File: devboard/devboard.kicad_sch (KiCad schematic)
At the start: 22 parts, among them J1 USB_C_Receptacle_USB2.0_14P, U1 RP2040, U2 NCP1117-3.3_SOT223, Y1 Crystal_GND24

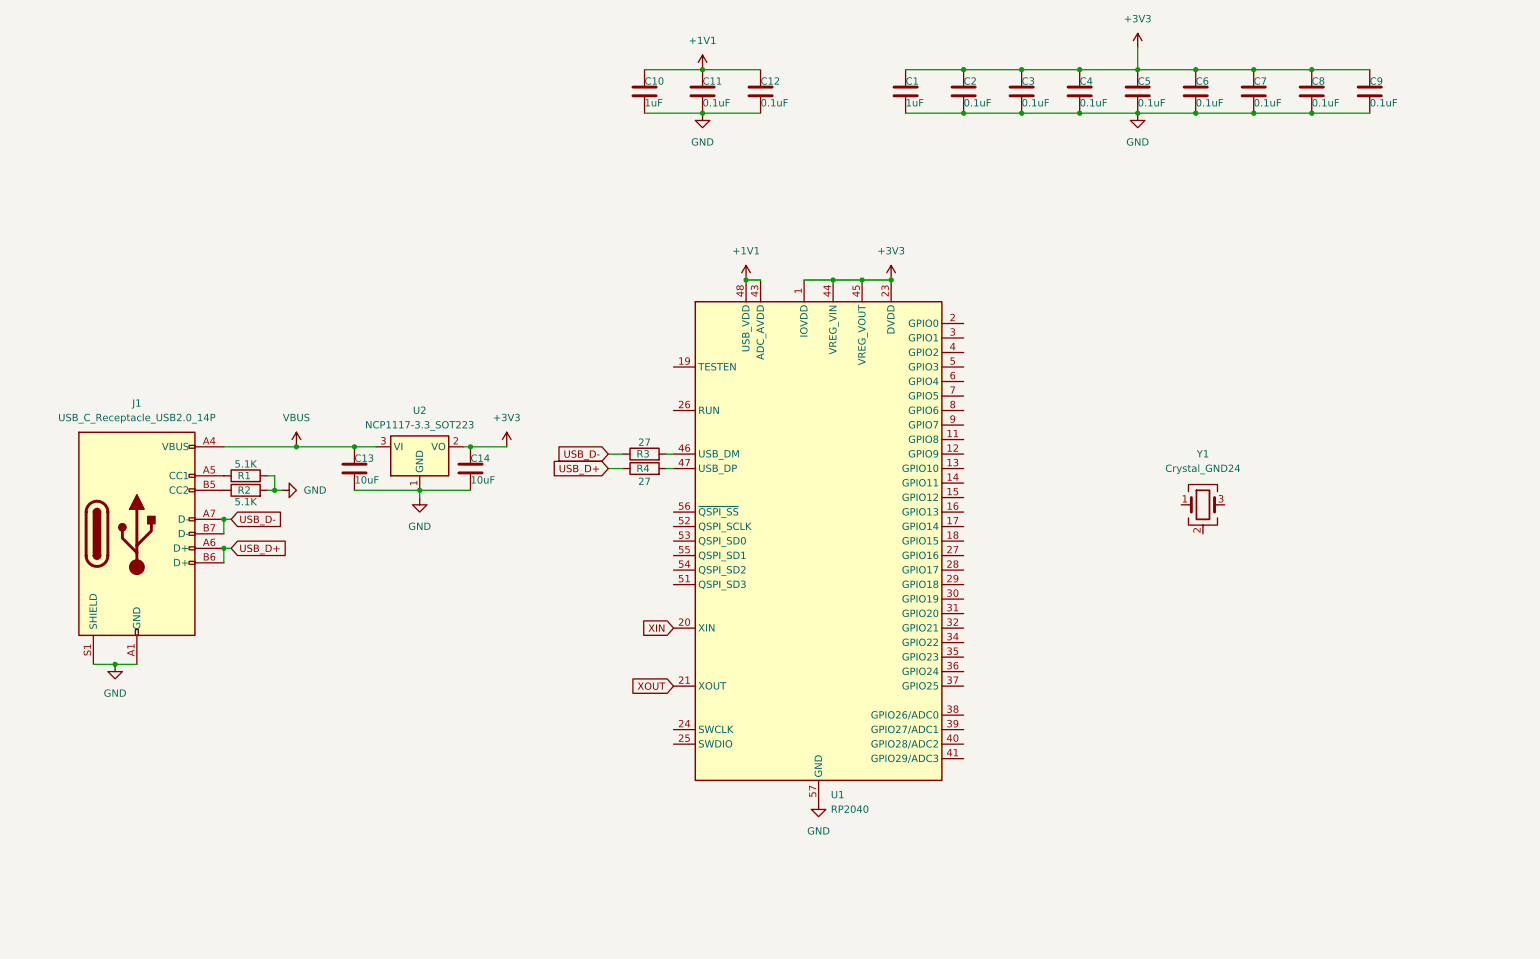
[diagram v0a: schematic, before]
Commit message: Finished basic schematic of Devboard 1.0
The schematics of the devboard with basic functionalities was finished.
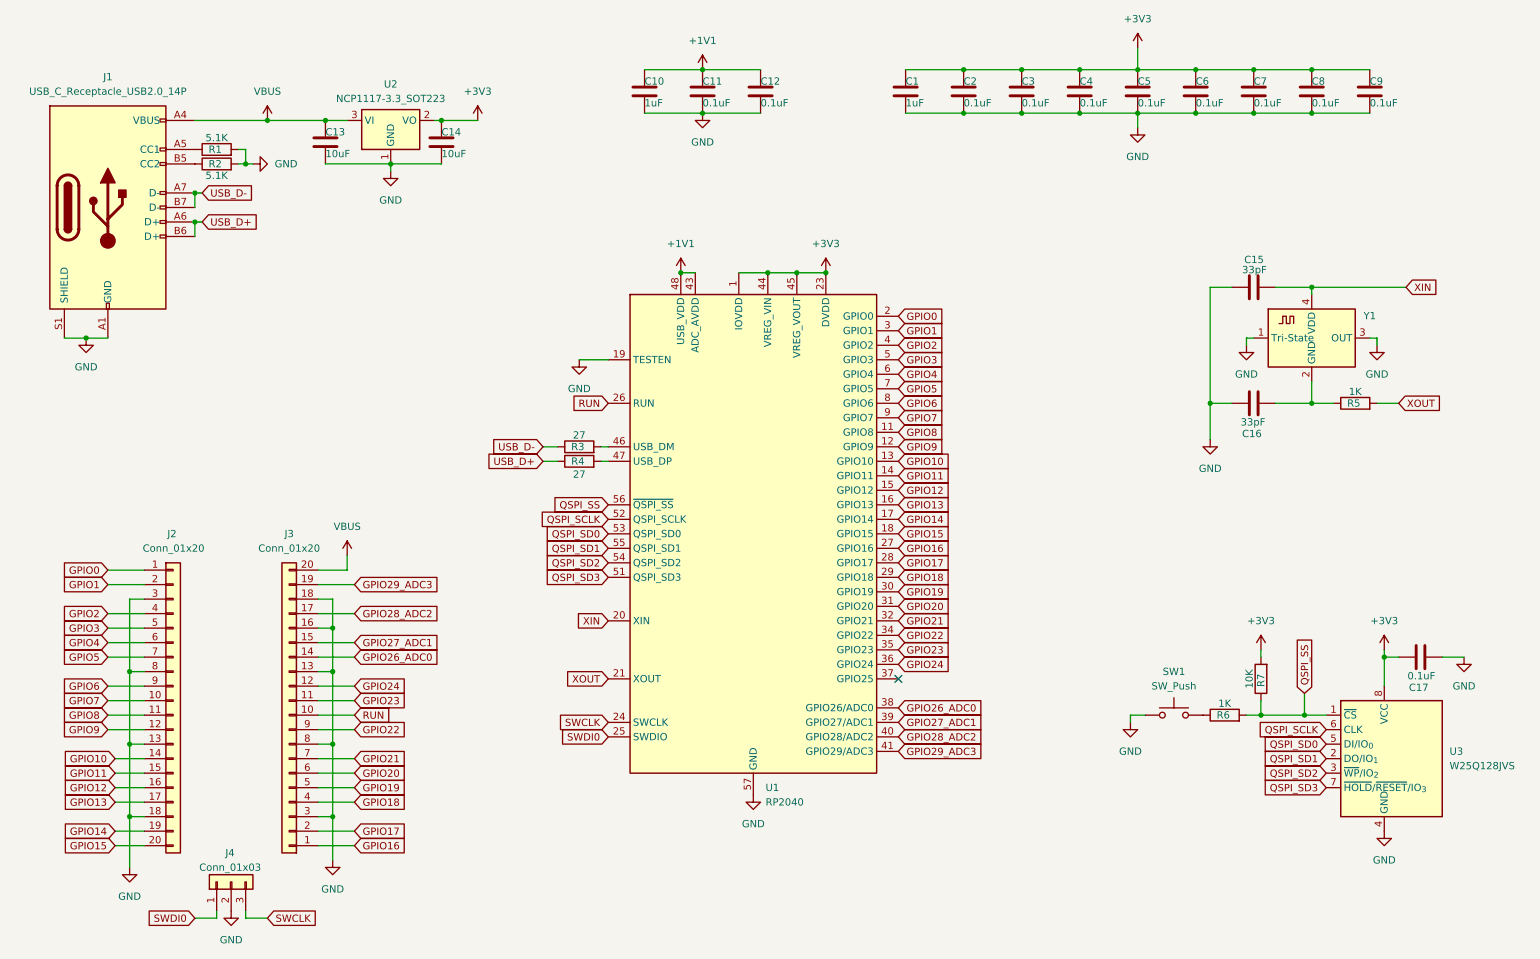
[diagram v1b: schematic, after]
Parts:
- removed Y1: Crystal_GND24, symbol Device:Crystal_GND24
- added C15, C16: 33pF, Capacitor_SMD:C_0402_1005Metric, symbol Device:C
- added C17: 0.1uF, Capacitor_SMD:C_0402_1005Metric, symbol Device:C
- added J2, J3: Conn_01x20, Connector_PinHeader_2.54mm:PinHeader_1x20_P2.54mm_Vertical, symbol Connector_Generic:Conn_01x20
- added J4: Conn_01x03, Connector_PinHeader_2.54mm:PinHeader_1x03_P2.54mm_Vertical, symbol Connector_Generic:Conn_01x03
- added R5, R6: 1K, Resistor_SMD:R_0402_1005Metric, symbol Device:R
- added R7: 10K, Resistor_SMD:R_0402_1005Metric, symbol Device:R
- added SW1: SW_Push, Button_Switch_SMD:SW_Push_SPST_NO_Alps_SKRK, symbol Switch:SW_Push
- added U3: W25Q128JVS, Package_SO:SOIC-8_5.3x5.3mm_P1.27mm, symbol Memory_Flash:W25Q128JVS
- added Y1: ASCO, Crystal:Crystal_SMD_3225-4Pin_3.2x2.5mm, symbol Oscillator:ASCO
- C1, C10, C11, C12, C2, C3, C4, C5, C6, C7, C8, C9: footprint (none) -> Capacitor_SMD:C_0402_1005Metric
- C13, C14: footprint (none) -> Capacitor_SMD:C_0201_0603Metric
- J1: footprint (none) -> Connector_USB:USB_C_Receptacle_HRO_TYPE-C-31-M-12
- R1, R2, R3, R4: footprint (none) -> Resistor_SMD:R_0402_1005Metric
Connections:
- net +3V3: now also C17.2, R7.2, U3.8 (VCC)
- net GND: now also U1.19 (TESTEN), C15.1, C16.2, C17.1, J2.13 (Pin_13), J2.18 (Pin_18), J2.3 (Pin_3), J2.8 (Pin_8), J3.13 (Pin_13), J3.16 (Pin_16), J3.18 (Pin_18), J3.3 (Pin_3), J3.8 (Pin_8), J4.2 (Pin_2), SW1.1, U3.4 (GND), Y1.1 (Tri-State), Y1.3 (OUT)
- net VBUS: now also J3.20 (Pin_20)
- net XIN: now also C15.2, Y1.4 (VDD)
- net XOUT: now also R5.2
- net GPIO8: now reaches U1.11 (GPIO8)
- net GPIO8: now also J2.11 (Pin_11)
- net GPIO9: now reaches U1.12 (GPIO9)
- net GPIO9: now also J2.12 (Pin_12)
- net GPIO10: now reaches U1.13 (GPIO10)
- net GPIO10: now also J2.14 (Pin_14)
- net GPIO11: now reaches U1.14 (GPIO11)
- net GPIO11: now also J2.15 (Pin_15)
- net GPIO12: now reaches U1.15 (GPIO12)
- net GPIO12: now also J2.16 (Pin_16)
- net GPIO13: now reaches U1.16 (GPIO13)
- net GPIO13: now also J2.17 (Pin_17)
- net GPIO14: now reaches U1.17 (GPIO14)
- net GPIO14: now also J2.19 (Pin_19)
- net GPIO15: now reaches U1.18 (GPIO15)
- net GPIO15: now also J2.20 (Pin_20)
- net GPIO0: now reaches U1.2 (GPIO0)
- net GPIO0: now also J2.1 (Pin_1)
- net SWCLK: now reaches U1.24 (SWCLK)
- net SWCLK: now also J4.3 (Pin_3)
- net SWDI0: now reaches U1.25 (SWDIO)
- net SWDI0: now also J4.1 (Pin_1)
- net RUN: now reaches U1.26 (RUN)
- net RUN: now also J3.10 (Pin_10)
- net GPIO16: now reaches U1.27 (GPIO16)
- net GPIO16: now also J3.1 (Pin_1)
- net GPIO17: now reaches U1.28 (GPIO17)
- net GPIO17: now also J3.2 (Pin_2)
- net GPIO18: now reaches U1.29 (GPIO18)
- net GPIO18: now also J3.4 (Pin_4)
- net GPIO1: now reaches U1.3 (GPIO1)
- net GPIO1: now also J2.2 (Pin_2)
- net GPIO19: now reaches U1.30 (GPIO19)
- net GPIO19: now also J3.5 (Pin_5)
- net GPIO20: now reaches U1.31 (GPIO20)
- net GPIO20: now also J3.6 (Pin_6)
- net GPIO21: now reaches U1.32 (GPIO21)
- net GPIO21: now also J3.7 (Pin_7)
- net GPIO22: now reaches U1.34 (GPIO22)
- net GPIO22: now also J3.9 (Pin_9)
- net GPIO23: now reaches U1.35 (GPIO23)
- net GPIO23: now also J3.11 (Pin_11)
- net GPIO24: now reaches U1.36 (GPIO24)
- net GPIO24: now also J3.12 (Pin_12)
- net GPIO26_ADC0: now reaches U1.38 (GPIO26/ADC0)
- net GPIO26_ADC0: now also J3.14 (Pin_14)
- net GPIO27_ADC1: now reaches U1.39 (GPIO27/ADC1)
- net GPIO27_ADC1: now also J3.15 (Pin_15)
- net GPIO2: now reaches U1.4 (GPIO2)
- net GPIO2: now also J2.4 (Pin_4)
- net GPIO28_ADC2: now reaches U1.40 (GPIO28/ADC2)
- net GPIO28_ADC2: now also J3.17 (Pin_17)
- net GPIO29_ADC3: now reaches U1.41 (GPIO29/ADC3)
- net GPIO29_ADC3: now also J3.19 (Pin_19)
- net GPIO3: now reaches U1.5 (GPIO3)
- net GPIO3: now also J2.5 (Pin_5)
- net QSPI_SD3: now reaches U1.51 (QSPI_SD3)
- net QSPI_SD3: now also U3.7 (~{HOLD}/~{RESET}/IO_{3})
- net QSPI_SCLK: now reaches U1.52 (QSPI_SCLK)
- net QSPI_SCLK: now also U3.6 (CLK)
- net QSPI_SD0: now reaches U1.53 (QSPI_SD0)
- net QSPI_SD0: now also U3.5 (DI/IO_{0})
- net QSPI_SD2: now reaches U1.54 (QSPI_SD2)
- net QSPI_SD2: now also U3.3 (~{WP}/IO_{2})
- net QSPI_SD1: now reaches U1.55 (QSPI_SD1)
- net QSPI_SD1: now also U3.2 (DO/IO_{1})
- net QSPI_SS: now reaches U1.56 (~{QSPI_SS})
- net QSPI_SS: now also R6.2, R7.1, U3.1 (~{CS})
- net GPIO4: now reaches U1.6 (GPIO4)
- net GPIO4: now also J2.6 (Pin_6)
- net GPIO5: now reaches U1.7 (GPIO5)
- net GPIO5: now also J2.7 (Pin_7)
- net GPIO6: now reaches U1.8 (GPIO6)
- net GPIO6: now also J2.9 (Pin_9)
- net GPIO7: now reaches U1.9 (GPIO7)
- net GPIO7: now also J2.10 (Pin_10)
- new net: R6.1, SW1.2
- new net: C16.1, R5.1, Y1.2 (GND)
- no-connect marks 0 -> 1
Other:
- title: (none) -> LeCalm Devboard
- moved on the sheet: C13, C14, J1, R1, R2, R3, R4, U1, U2

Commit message: PCB routing and changes
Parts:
- removed U2: NCP1117-3.3_SOT223, Package_TO_SOT_SMD:SOT-223-3_TabPin2, symbol Regulator_Linear:NCP1117-3.3_SOT223
- added U2: MCP1700x-120xxTT, Package_TO_SOT_SMD:SOT-23, symbol Regulator_Linear:MCP1700x-120xxTT
- U3: footprint Package_SO:SOIC-8_5.3x5.3mm_P1.27mm -> Package_SON:Winbond_USON-8-1EP_3x2mm_P0.5mm_EP0.2x1.6mm
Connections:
- net +3V3: now also U2.2 (VO)
- net GND: now also Y1.2 (GND), Y1.4 (VDD), U2.1 (GND); no longer Y1.1 (Tri-State), Y1.3 (OUT)
- net VBUS: now also U2.3 (VI)
- net XIN: now also Y1.3 (OUT); no longer Y1.4 (VDD)
- net at C16.1, R5.1: now also Y1.1 (Tri-State); no longer Y1.2 (GND)
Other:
- moved on the sheet: C15, C16, R5, Y1
